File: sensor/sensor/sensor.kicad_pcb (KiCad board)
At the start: 4 copper layers, 72.2 x 21 mm, 59 parts, among them IC1 VL53L4CDV0DH_1, IC2 ISL29125IROZ-T7, J1 RJ12_Shielded, J2 Conn_01x04, J3 Conn_01x06, J8 RJ12_Shielded, J9 Conn_01x06, SW5 SW_Coded_SH-7050, U1 PCA9615DP, U2 LTC4316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

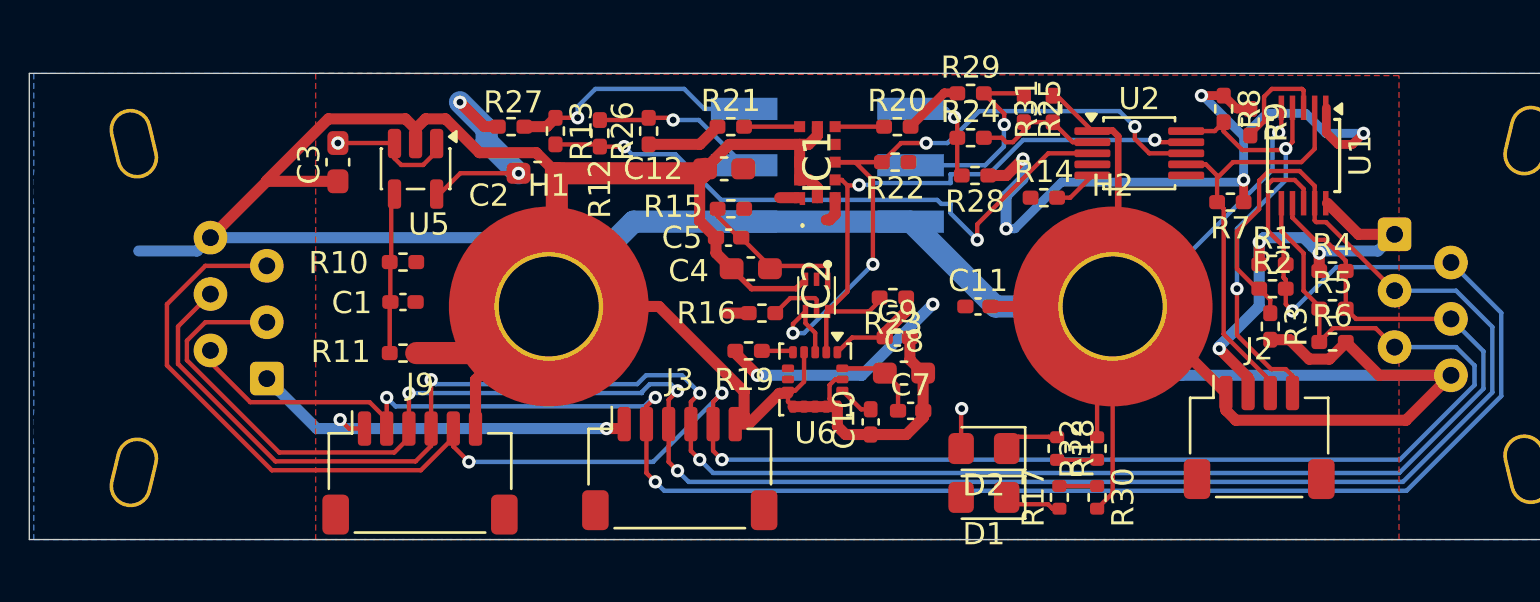
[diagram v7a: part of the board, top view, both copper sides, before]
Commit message: sensor pcb layout
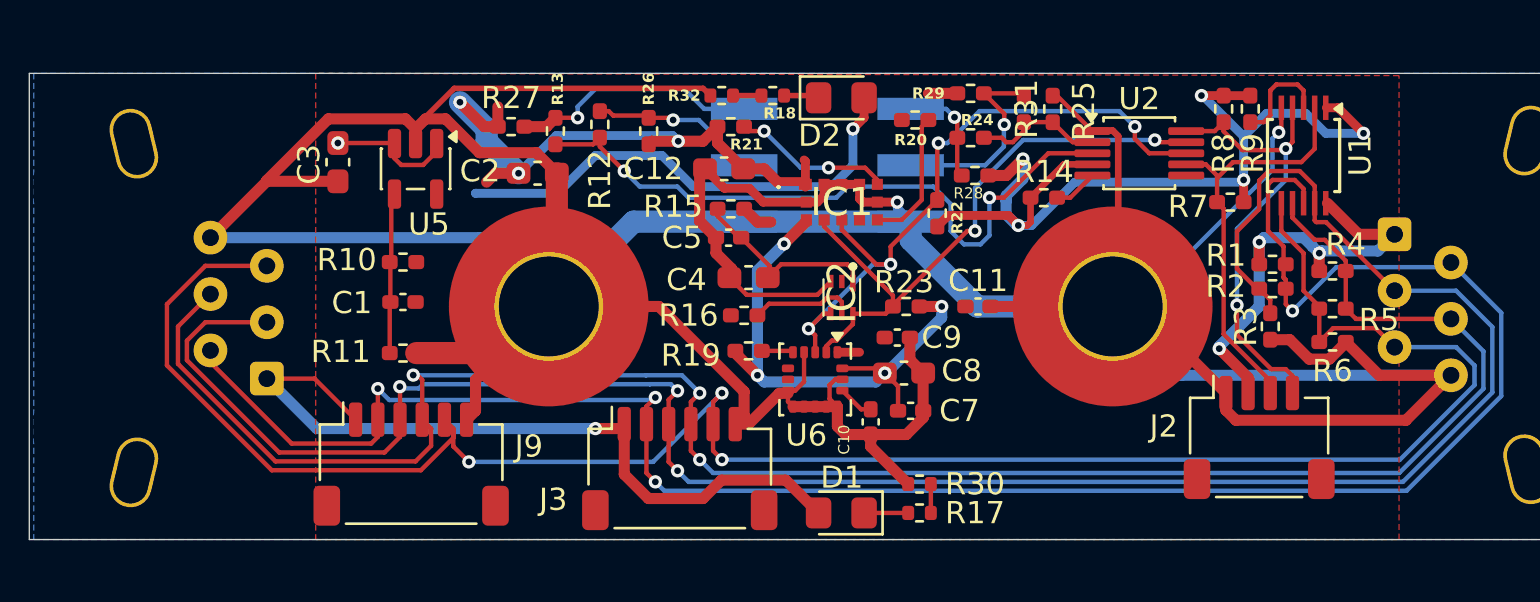
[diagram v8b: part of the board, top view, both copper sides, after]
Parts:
- moved R32 23.2 mm to (96.3, 84.8), turned to 180 degrees
- moved R18 20.4 mm to (98.6, 84.8), turned to 180 degrees
- moved D2 17.1 mm to (101.7, 84.9), turned to 0 degrees
- moved R30 8.02 mm to (105.2, 102.3), turned to 180 degrees
- moved D1 6.46 mm to (101.7, 103.6)
- moved R17 6.34 mm to (105.2, 103.6), turned to 0 degrees
- moved R22 2.98 mm to (106.0, 90.1), turned to 90 degrees
- moved IC1 2.11 mm to (101.7, 89.6), turned to 180 degrees
- moved IC2 1.14 mm to (101.7, 93.9)
- moved R20 0.86 mm to (105.0, 85.9), turned to 180 degrees
- moved R16 0.81 mm to (97.3, 94.7)
- moved R23 0.72 mm to (104.6, 94.3)
- moved R9 0.60 mm to (120.1, 85.4)
- moved J9 0.57 mm to (82.3, 101.4)
- moved C4 0.41 mm to (97.5, 93.0)
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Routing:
- net +5V: track 46.4 -> 82.4 mm, vias 7 -> 6
- net +3.3V: track 73.5 -> 97.1 mm, vias 9 -> 12
- net Net-(IC1-XSHUT): track 2.50 -> 7.20 mm, vias 0 -> 2
- net Net-(IC1-GPIO1): track 2.20 -> 6.10 mm
- net GND: track 240.2 -> 236.8 mm, vias 1 -> 2
- net Net-(U2-XORL): track 28.2 -> 30.4 mm
- net Net-(IC2-~{INT}): track 2.70 -> 4.74 mm
- net Net-(IC2-VDD): track 7.02 -> 8.97 mm
- net /Sensors/sda: track 31.8 -> 29.9 mm
- net Net-(J3-Pin_4): track 88.1 -> 89.3 mm
- net Net-(D2-K): track 2.50 -> 1.59 mm
- net Net-(J3-Pin_2): track 91.8 -> 92.6 mm
- net /Sensors/scl: track 27.6 -> 27.0 mm
- net Net-(D1-K): track 2.59 -> 1.99 mm
- net Net-(J3-Pin_5): track 92.7 -> 93.3 mm
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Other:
- copper layers 4 -> 2
